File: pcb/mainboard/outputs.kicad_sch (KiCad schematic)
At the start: 47 parts, among them U38 ISL24021IRT065Z-T7A‎, U39 ISL24021IRT065Z-T7A‎, U40 ISL24021IRT065Z-T7A‎, U41 ISL24021IRT065Z-T7A‎, U42 DACx0508_WQFN, U43 ISL24021IRT065Z-T7A‎, U44 ISL24021IRT065Z-T7A‎, U45 ISL24021IRT065Z-T7A‎, U46 ISL24021IRT065Z-T7A‎, U8 XC7K70T-2FBG484C

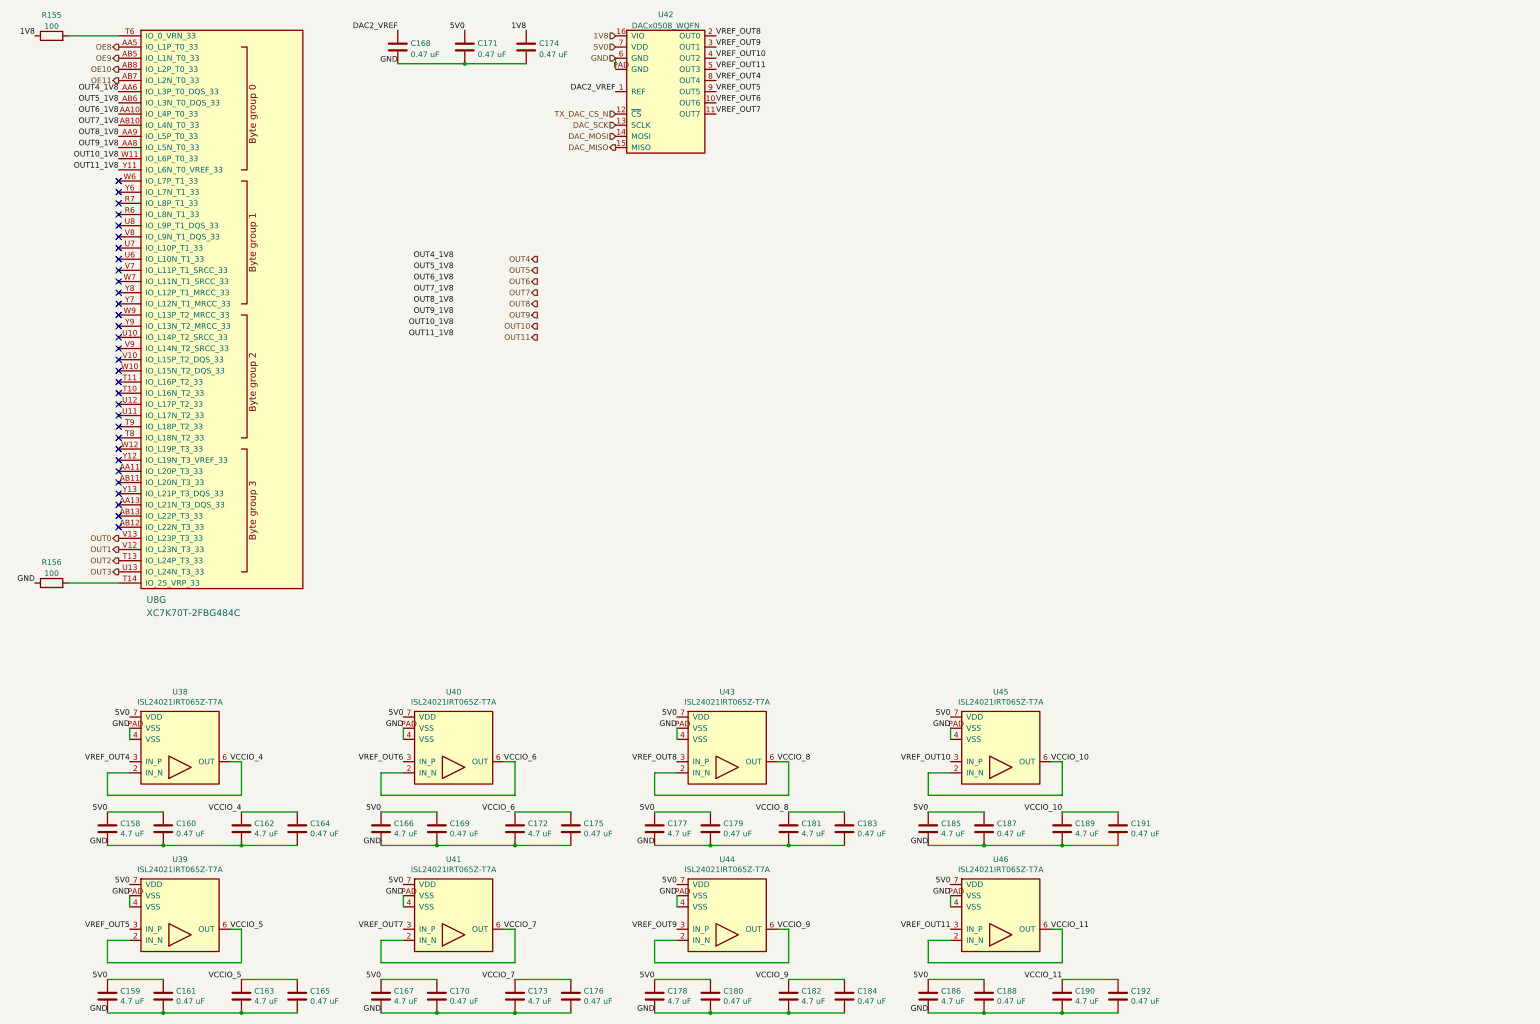
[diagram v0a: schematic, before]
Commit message: Finished initial iteration of schematic, needs a verification pass to check for missing features then schematic review
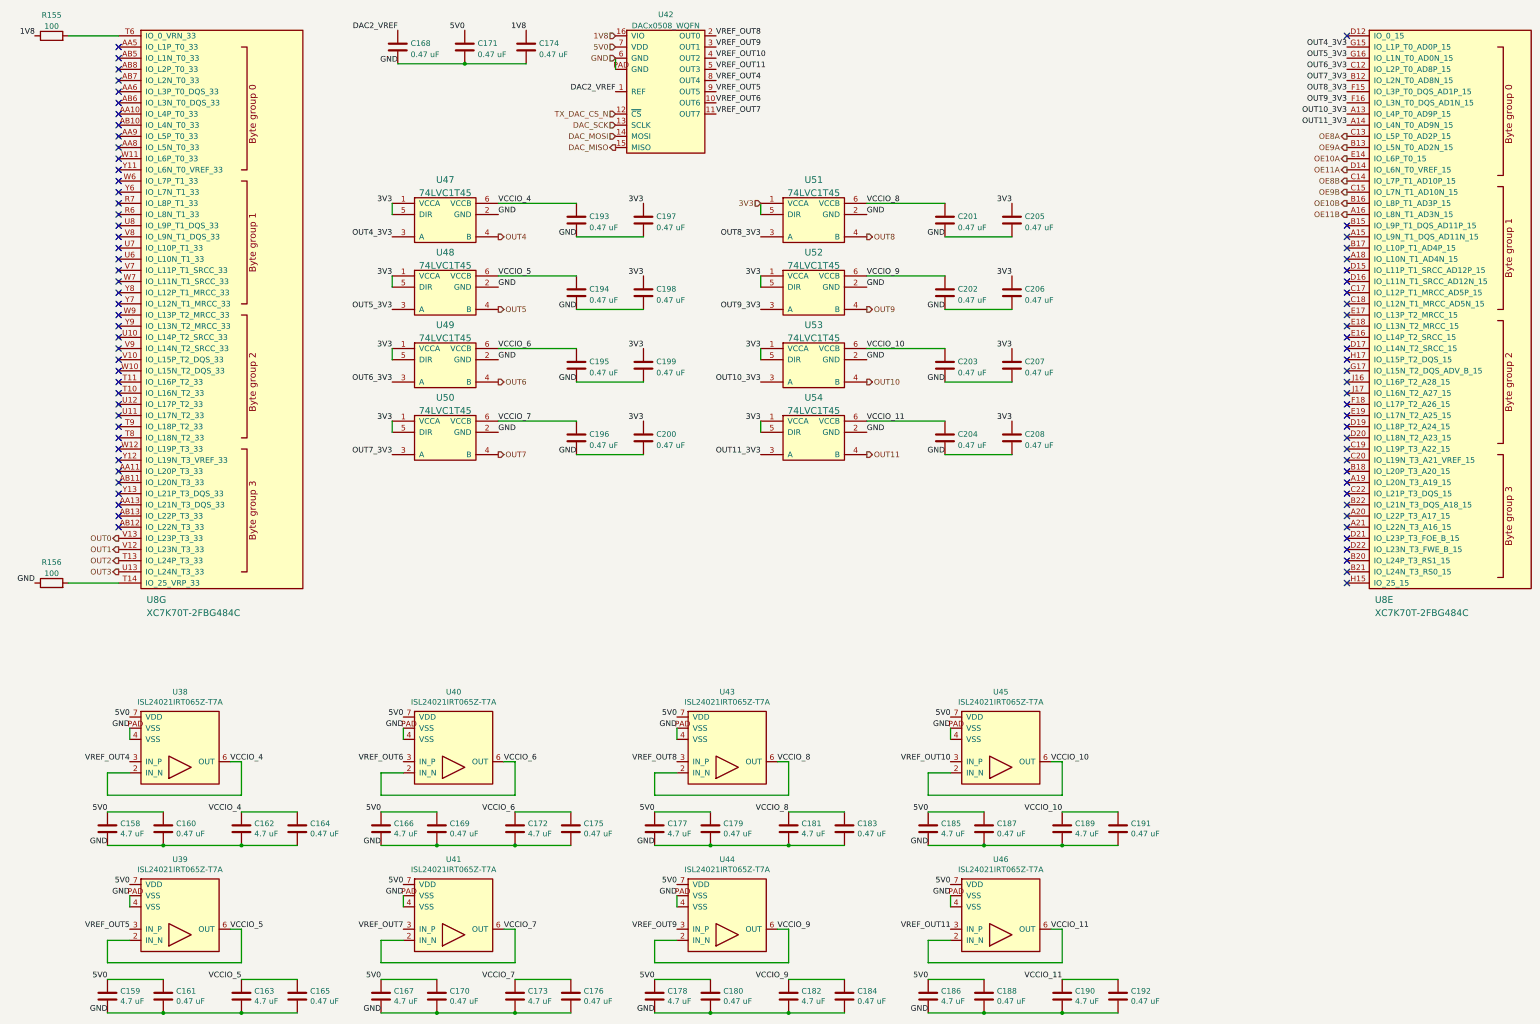
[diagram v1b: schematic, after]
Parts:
- added C193, C194, C195, C196, C197, C198, C199, C200, C201, C202, C203, C204, C205, C206, C207, C208: 0.47 uF, symbol device:C
- added U47, U48, U49, U50, U51, U52, U53, U54: 74LVC1T45, symbol special-azonenberg:74AVC1T45
- added unit 5 of U8
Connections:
- net GND: now also C193.2, C194.2, C195.2, C196.2, C197.2, C198.2, C199.2, C200.2, C201.2, C202.2, C203.2, C204.2, C205.2, C206.2, C207.2, C208.2, U47.2 (GND), U48.2 (GND), U49.2 (GND), U50.2 (GND), U51.2 (GND), U52.2 (GND), U53.2 (GND), U54.2 (GND)
- net OUT10: now also U53.4 (B)
- net OUT11: now also U54.4 (B)
- net OUT4: now also U47.4 (B)
- net OUT5: now also U48.4 (B)
- net OUT6: now also U49.4 (B)
- net OUT7: now also U50.4 (B)
- net OUT8: now also U51.4 (B)
- net OUT9: now also U52.4 (B)
- net VCCIO_10: now also C203.1, U53.6 (VCCB)
- net VCCIO_11: now also C204.1, U54.6 (VCCB)
- net VCCIO_4: now also C193.1, U47.6 (VCCB)
- net VCCIO_5: now also C194.1, U48.6 (VCCB)
- net VCCIO_6: now also C195.1, U49.6 (VCCB)
- net VCCIO_7: now also C196.1, U50.6 (VCCB)
- net VCCIO_8: now also C201.1, U51.6 (VCCB)
- net VCCIO_9: now also C202.1, U52.6 (VCCB)
- net OE10: no longer names the net of U8.AB8 (IO_L2P_T0_33)
- net OE11: no longer names the net of U8.AB7 (IO_L2N_T0_33)
- net OE8: no longer names the net of U8.AA5 (IO_L1P_T0_33)
- net OE9: no longer names the net of U8.AB5 (IO_L1N_T0_33)
- net OUT10_1V8: no longer names the net of U8.W11 (IO_L6P_T0_33)
- net OUT11_1V8: no longer names the net of U8.Y11 (IO_L6N_T0_VREF_33)
- net OUT4_1V8: no longer names the net of U8.AA6 (IO_L3P_T0_DQS_33)
- net OUT5_1V8: no longer names the net of U8.AB6 (IO_L3N_T0_DQS_33)
- net OUT6_1V8: no longer names the net of U8.AA10 (IO_L4P_T0_33)
- net OUT7_1V8: no longer names the net of U8.AB10 (IO_L4N_T0_33)
- net OUT8_1V8: no longer names the net of U8.AA9 (IO_L5P_T0_33)
- net OUT9_1V8: no longer names the net of U8.AA8 (IO_L5N_T0_33)
- new net 3V3: C197.1, C198.1, C199.1, C200.1, C205.1, C206.1, C207.1, C208.1, U47.1 (VCCA), U47.5 (DIR), U48.1 (VCCA), U48.5 (DIR), U49.1 (VCCA), U49.5 (DIR), U50.1 (VCCA), U50.5 (DIR), U51.1 (VCCA), U51.5 (DIR), U52.1 (VCCA), U52.5 (DIR), U53.1 (VCCA), U53.5 (DIR), U54.1 (VCCA), U54.5 (DIR)
- new net OE10A: U8.E14 (IO_L6P_T0_15)
- new net OE10B: U8.B16 (IO_L8P_T1_AD3P_15)
- new net OE11A: U8.D14 (IO_L6N_T0_VREF_15)
- new net OE11B: U8.A16 (IO_L8N_T1_AD3N_15)
- new net OE8A: U8.C13 (IO_L5P_T0_AD2P_15)
- new net OE8B: U8.C14 (IO_L7P_T1_AD10P_15)
- new net OE9A: U8.B13 (IO_L5N_T0_AD2N_15)
- new net OE9B: U8.C15 (IO_L7N_T1_AD10N_15)
- new net OUT10_3V3: U53.3 (A), U8.A13 (IO_L4P_T0_AD9P_15)
- new net OUT11_3V3: U54.3 (A), U8.A14 (IO_L4N_T0_AD9N_15)
- new net OUT4_3V3: U47.3 (A), U8.G15 (IO_L1P_T0_AD0P_15)
- new net OUT5_3V3: U48.3 (A), U8.G16 (IO_L1N_T0_AD0N_15)
- new net OUT6_3V3: U49.3 (A), U8.C12 (IO_L2P_T0_AD8P_15)
- new net OUT7_3V3: U50.3 (A), U8.B12 (IO_L2N_T0_AD8N_15)
- new net OUT8_3V3: U51.3 (A), U8.F15 (IO_L3P_T0_DQS_AD1P_15)
- new net OUT9_3V3: U52.3 (A), U8.F16 (IO_L3N_T0_DQS_AD1N_15)
- no-connect marks 32 -> 78

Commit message: Calculated power monitor voltage divider
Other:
- company: (none) -> Antikernel Labs
- title: (none) -> Trigger Crossbar
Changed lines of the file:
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@@
 (kicad_sch (version 20211123) (generator eeschema)
   (paper "A3")
+  (title_block
+    (title "Trigger Crossbar")
+    (date "2023-12-17")
+    (rev "0.1")
+    (company "Antikernel Labs")
+    (comment 1 "Andrew D. Zonenberg")
+  )
   (junction (at 142.24 248.92) (diameter 0) (color 0 0 0 0)
   )

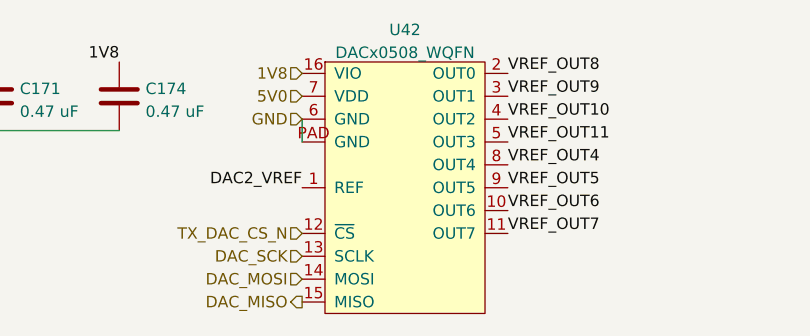
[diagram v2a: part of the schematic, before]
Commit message: Began assigning footprints
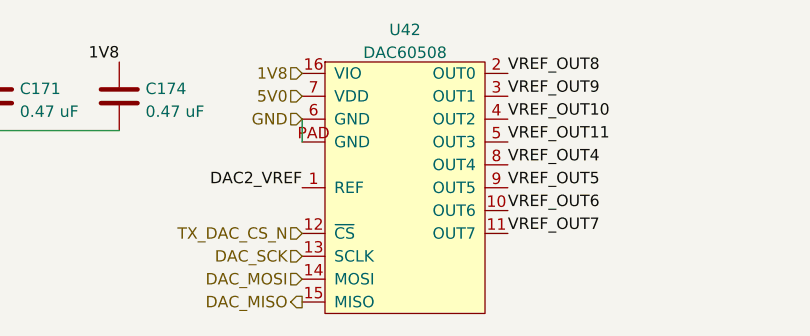
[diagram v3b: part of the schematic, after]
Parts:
- C168, C171, C174, C193, C194, C195, C196, C197, C198, C199, C200, C201, C202, C203, C204, C205, C206, C207, C208: footprint (none) -> azonenberg_pcb:EIA_0402_CAP_NOSILK
- R155, R156: footprint (none) -> azonenberg_pcb:EIA_0402_RES_NOSILK
- U42: value DACx0508_WQFN -> DAC60508; footprint (none) -> azonenberg_pcb:QFN_16_0.5MM_3x3MM
- U8: footprint (none) -> azonenberg_pcb:BGA_484_22x22_FULLARRAY_1MM
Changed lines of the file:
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@@
     (in_bom yes) (on_board yes) (fields_autoplaced)
     (property "Reference" "U42" (id 0) (at 194.31 21.8272 0))
-    (property "Value" "DACx0508_WQFN" (id 1) (at 194.31 24.3641 0))
-    (property "Footprint" "" (id 2) (at 185.42 53.34 0)
+    (property "Value" "DAC60508" (id 1) (at 194.31 24.3641 0))
+    (property "Footprint" "azonenberg_pcb:QFN_16_0.5MM_3x3MM" (id 2) (at 185.42 53.34 0)
       (effects (font (size 1.27 1.27)) hide)
     )
@@
       (effects (font (size 1.27 1.27)) (justify left))
     )
-    (property "Footprint" "" (id 2) (at 190.1952 105.41 0)
+    (property "Footprint" "azonenberg_pcb:EIA_0402_CAP_NOSILK" (id 2) (at 190.1952 105.41 0)
       (effects (font (size 1.27 1.27)) hide)
     )
@@
       (effects (font (size 1.27 1.27)) (justify left))
     )
-    (property "Footprint" "" (id 2) (at 134.3152 33.02 0)
+    (property "Footprint" "azonenberg_pcb:EIA_0402_CAP_NOSILK" (id 2) (at 134.3152 33.02 0)
       (effects (font (size 1.27 1.27)) hide)
     )
@@
       (effects (font (size 1.27 1.27)) (justify left))
     )
-    (property "Footprint" "" (id 2) (at 258.7752 72.39 0)
+    (property "Footprint" "azonenberg_pcb:EIA_0402_CAP_NOSILK" (id 2) (at 258.7752 72.39 0)
       (effects (font (size 1.27 1.27)) hide)
     )
@@
       (effects (font (size 1.27 1.27)) (justify left))
     )
-    (property "Footprint" "" (id 2) (at 174.9552 105.41 0)
+    (property "Footprint" "azonenberg_pcb:EIA_0402_CAP_NOSILK" (id 2) (at 174.9552 105.41 0)
       (effects (font (size 1.27 1.27)) hide)
     )
@@
       (effects (font (size 1.524 1.524)) (justify left))
     )
-    (property "Footprint" "" (id 2) (at 354.33 158.75 0)
+    (property "Footprint" "azonenberg_pcb:BGA_484_22x22_FULLARRAY_1MM" (id 2) (at 354.33 158.75 0)
       (effects (font (size 1.524 1.524)) hide)
     )
@@
       (effects (font (size 1.27 1.27)) (justify left))
     )
-    (property "Footprint" "" (id 2) (at 163.5252 33.02 0)
+    (property "Footprint" "azonenberg_pcb:EIA_0402_CAP_NOSILK" (id 2) (at 163.5252 33.02 0)
       (effects (font (size 1.27 1.27)) hide)
     )
@@
       (effects (font (size 1.27 1.27)) (justify left))
     )
-    (property "Footprint" "" (id 2) (at 274.0152 121.92 0)
+    (property "Footprint" "azonenberg_pcb:EIA_0402_CAP_NOSILK" (id 2) (at 274.0152 121.92 0)
       (effects (font (size 1.27 1.27)) hide)
     )
@@
       (effects (font (size 1.27 1.27)) (justify left))
     )
-    (property "Footprint" "" (id 2) (at 174.9552 121.92 0)
+    (property "Footprint" "azonenberg_pcb:EIA_0402_CAP_NOSILK" (id 2) (at 174.9552 121.92 0)
       (effects (font (size 1.27 1.27)) hide)
     )
@@
       (effects (font (size 1.524 1.524)) (justify left))
     )
-    (property "Footprint" "" (id 2) (at 74.93 158.75 0)
+    (property "Footprint" "azonenberg_pcb:BGA_484_22x22_FULLARRAY_1MM" (id 2) (at 74.93 158.75 0)
       (effects (font (size 1.524 1.524)) hide)
     )
@@
       (effects (font (size 1.27 1.27)) (justify left))
     )
-    (property "Footprint" "" (id 2) (at 274.0152 88.9 0)
+    (property "Footprint" "azonenberg_pcb:EIA_0402_CAP_NOSILK" (id 2) (at 274.0152 88.9 0)
       (effects (font (size 1.27 1.27)) hide)
     )
@@
       (effects (font (size 1.27 1.27)) (justify left))
     )
-    (property "Footprint" "" (id 2) (at 274.0152 105.41 0)
+    (property "Footprint" "azonenberg_pcb:EIA_0402_CAP_NOSILK" (id 2) (at 274.0152 105.41 0)
       (effects (font (size 1.27 1.27)) hide)
     )
@@
     (property "Reference" "R155" (id 0) (at 54.61 21.9542 90))
     (property "Value" "100" (id 1) (at 54.61 24.4911 90))
-    (property "Footprint" "" (id 2) (at 54.61 28.448 90)
+    (property "Footprint" "azonenberg_pcb:EIA_0402_RES_NOSILK" (id 2) (at 54.61 28.448 90)
       (effects (font (size 1.27 1.27)) hide)
     )
@@
       (effects (font (size 1.27 1.27)) (justify left))
     )
-    (property "Footprint" "" (id 2) (at 258.7752 121.92 0)
+    (property "Footprint" "azonenberg_pcb:EIA_0402_CAP_NOSILK" (id 2) (at 258.7752 121.92 0)
       (effects (font (size 1.27 1.27)) hide)
     )
@@
       (effects (font (size 1.27 1.27)) (justify left))
     )
-    (property "Footprint" "" (id 2) (at 274.0152 72.39 0)
+    (property "Footprint" "azonenberg_pcb:EIA_0402_CAP_NOSILK" (id 2) (at 274.0152 72.39 0)
       (effects (font (size 1.27 1.27)) hide)
     )
@@
       (effects (font (size 1.27 1.27)) (justify left))
     )
-    (property "Footprint" "" (id 2) (at 258.7752 88.9 0)
+    (property "Footprint" "azonenberg_pcb:EIA_0402_CAP_NOSILK" (id 2) (at 258.7752 88.9 0)
       (effects (font (size 1.27 1.27)) hide)
     )
@@
       (effects (font (size 1.27 1.27)) (justify left))
     )
-    (property "Footprint" "" (id 2) (at 174.9552 72.39 0)
+    (property "Footprint" "azonenberg_pcb:EIA_0402_CAP_NOSILK" (id 2) (at 174.9552 72.39 0)
       (effects (font (size 1.27 1.27)) hide)
     )
@@
       (effects (font (size 1.27 1.27)) (justify left))
     )
-    (property "Footprint" "" (id 2) (at 190.1952 88.9 0)
+    (property "Footprint" "azonenberg_pcb:EIA_0402_CAP_NOSILK" (id 2) (at 190.1952 88.9 0)
       (effects (font (size 1.27 1.27)) hide)
     )
@@
     (property "Reference" "R156" (id 0) (at 54.61 146.4142 90))
     (property "Value" "100" (id 1) (at 54.61 148.9511 90))
-    (property "Footprint" "" (id 2) (at 54.61 152.908 90)
+    (property "Footprint" "azonenberg_pcb:EIA_0402_RES_NOSILK" (id 2) (at 54.61 152.908 90)
       (effects (font (size 1.27 1.27)) hide)
     )
@@
       (effects (font (size 1.27 1.27)) (justify left))
     )
-    (property "Footprint" "" (id 2) (at 174.9552 88.9 0)
+    (property "Footprint" "azonenberg_pcb:EIA_0402_CAP_NOSILK" (id 2) (at 174.9552 88.9 0)
       (effects (font (size 1.27 1.27)) hide)
     )
@@
       (effects (font (size 1.27 1.27)) (justify left))
     )
-    (property "Footprint" "" (id 2) (at 190.1952 121.92 0)
+    (property "Footprint" "azonenberg_pcb:EIA_0402_CAP_NOSILK" (id 2) (at 190.1952 121.92 0)
       (effects (font (size 1.27 1.27)) hide)
     )
@@
       (effects (font (size 1.27 1.27)) (justify left))
     )
-    (property "Footprint" "" (id 2) (at 149.5552 33.02 0)
+    (property "Footprint" "azonenberg_pcb:EIA_0402_CAP_NOSILK" (id 2) (at 149.5552 33.02 0)
       (effects (font (size 1.27 1.27)) hide)
     )
@@
       (effects (font (size 1.27 1.27)) (justify left))
     )
-    (property "Footprint" "" (id 2) (at 258.7752 105.41 0)
+    (property "Footprint" "azonenberg_pcb:EIA_0402_CAP_NOSILK" (id 2) (at 258.7752 105.41 0)
       (effects (font (size 1.27 1.27)) hide)
     )
@@
       (effects (font (size 1.27 1.27)) (justify left))
     )
-    (property "Footprint" "" (id 2) (at 190.1952 72.39 0)
-      (effects (font (size 1.27 1.27)) hide)
-    )
+    (property "Footprint" "azonenberg_pcb:EIA_0402_CAP_NOSILK" (id 2) (at 190.1952 72.39 0)
+      (effects (font (size 1.27 1.27)) hide)
+    )

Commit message: Finished component footprint assignment, started some EM simulations. Ready for schematic review.
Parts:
- U47, U48, U49, U50, U51, U52, U53, U54: footprint (none) -> azonenberg_pcb:DFN_6_0.5MM_1.6x1.6MM_TI_DPK
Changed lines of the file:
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@@
   (title_block
     (title "Trigger Crossbar")
-    (date "2023-12-17")
+    (date "2023-12-18")
     (rev "0.1")
     (company "Antikernel Labs")
@@
       (effects (font (size 1.524 1.524)))
     )
-    (property "Footprint" "" (id 2) (at 220.98 90.17 0)
+    (property "Footprint" "azonenberg_pcb:DFN_6_0.5MM_1.6x1.6MM_TI_DPK" (id 2) (at 220.98 90.17 0)
       (effects (font (size 1.524 1.524)) hide)
     )
@@
       (effects (font (size 1.524 1.524)))
     )
-    (property "Footprint" "" (id 2) (at 137.16 73.66 0)
+    (property "Footprint" "azonenberg_pcb:DFN_6_0.5MM_1.6x1.6MM_TI_DPK" (id 2) (at 137.16 73.66 0)
       (effects (font (size 1.524 1.524)) hide)
     )
@@
       (effects (font (size 1.524 1.524)))
     )
-    (property "Footprint" "" (id 2) (at 137.16 106.68 0)
+    (property "Footprint" "azonenberg_pcb:DFN_6_0.5MM_1.6x1.6MM_TI_DPK" (id 2) (at 137.16 106.68 0)
       (effects (font (size 1.524 1.524)) hide)
     )
@@
       (effects (font (size 1.524 1.524)))
     )
-    (property "Footprint" "" (id 2) (at 137.16 123.19 0)
+    (property "Footprint" "azonenberg_pcb:DFN_6_0.5MM_1.6x1.6MM_TI_DPK" (id 2) (at 137.16 123.19 0)
       (effects (font (size 1.524 1.524)) hide)
     )
@@
       (effects (font (size 1.524 1.524)))
     )
-    (property "Footprint" "" (id 2) (at 220.98 73.66 0)
+    (property "Footprint" "azonenberg_pcb:DFN_6_0.5MM_1.6x1.6MM_TI_DPK" (id 2) (at 220.98 73.66 0)
       (effects (font (size 1.524 1.524)) hide)
     )
@@
       (effects (font (size 1.524 1.524)))
     )
-    (property "Footprint" "" (id 2) (at 220.98 106.68 0)
+    (property "Footprint" "azonenberg_pcb:DFN_6_0.5MM_1.6x1.6MM_TI_DPK" (id 2) (at 220.98 106.68 0)
       (effects (font (size 1.524 1.524)) hide)
     )
@@
       (effects (font (size 1.524 1.524)))
     )
-    (property "Footprint" "" (id 2) (at 137.16 90.17 0)
+    (property "Footprint" "azonenberg_pcb:DFN_6_0.5MM_1.6x1.6MM_TI_DPK" (id 2) (at 137.16 90.17 0)
       (effects (font (size 1.524 1.524)) hide)
     )
@@
       (effects (font (size 1.524 1.524)))
     )
-    (property "Footprint" "" (id 2) (at 220.98 123.19 0)
+    (property "Footprint" "azonenberg_pcb:DFN_6_0.5MM_1.6x1.6MM_TI_DPK" (id 2) (at 220.98 123.19 0)
       (effects (font (size 1.524 1.524)) hide)
     )
